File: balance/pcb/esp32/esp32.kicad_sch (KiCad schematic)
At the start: 3 parts

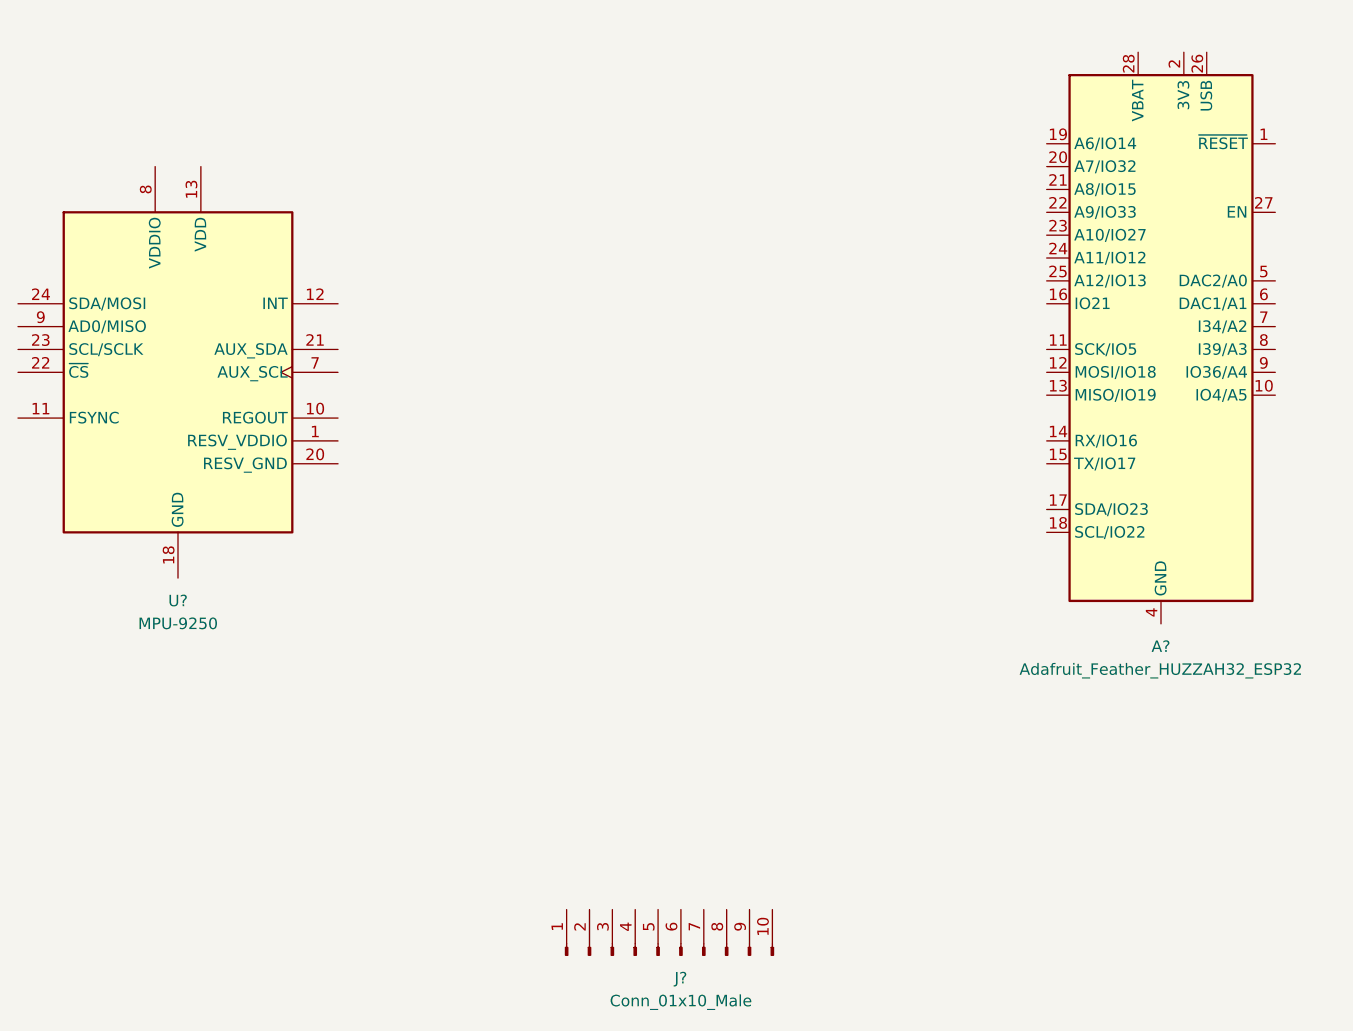
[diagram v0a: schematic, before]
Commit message: balance robot: power board
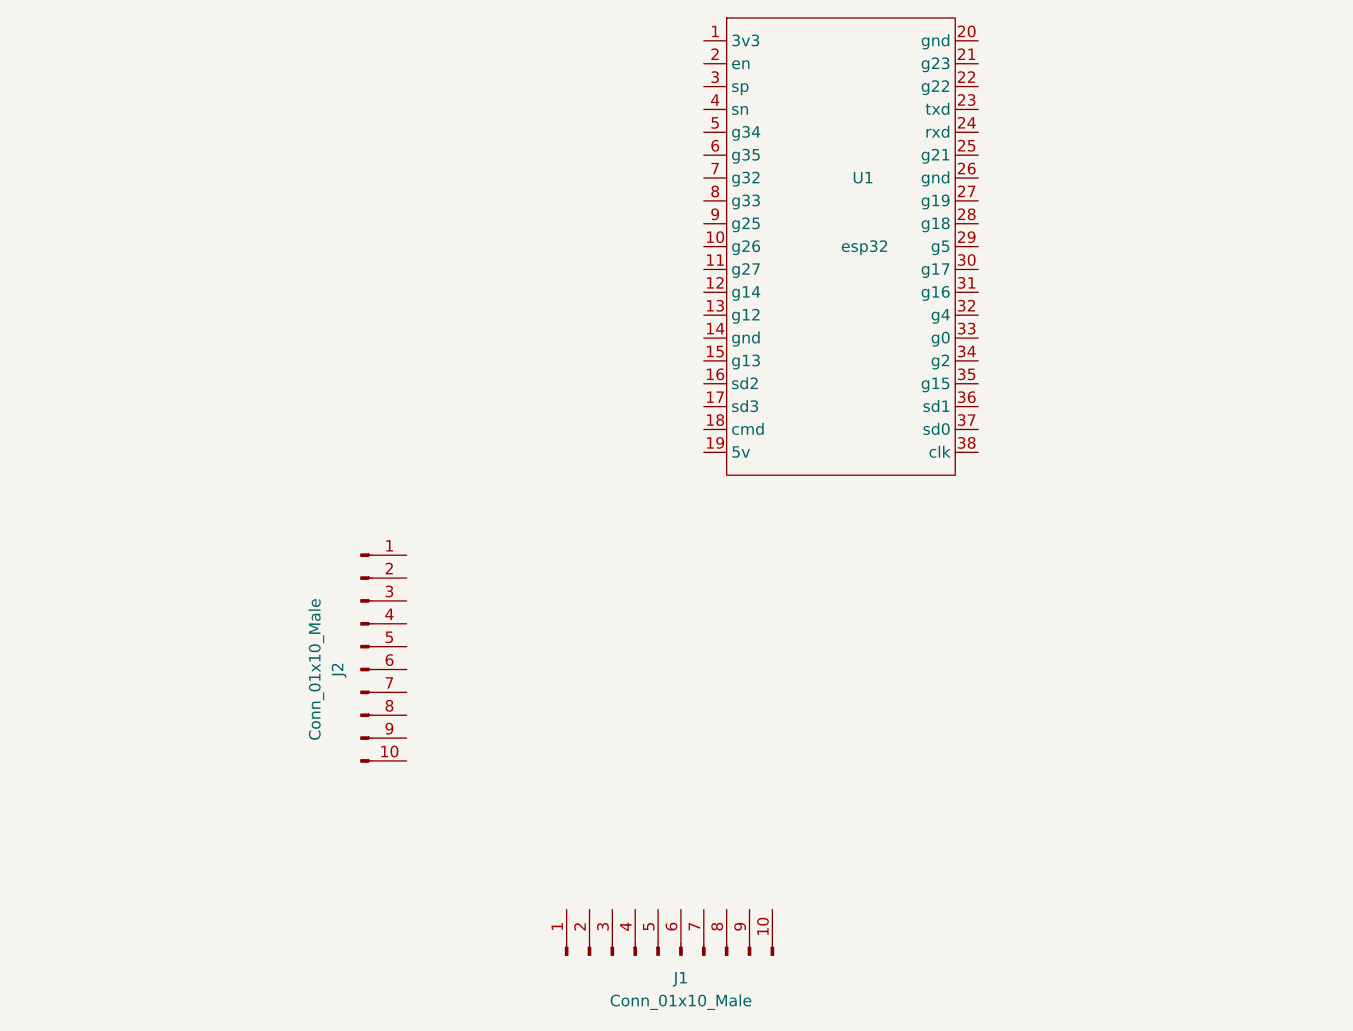
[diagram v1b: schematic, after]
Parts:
- removed A?: Adafruit_Feather_HUZZAH32_ESP32, Module:Adafruit_Feather, symbol MCU_Module:Adafruit_Feather_HUZZAH32_ESP32
- removed U?: MPU-9250, Sensor_Motion:InvenSense_QFN-24_3x3mm_P0.4mm, symbol Sensor_Motion:MPU-9250
- added J2: Conn_01x10_Male, Connector_PinHeader_2.54mm:PinHeader_1x10_P2.54mm_Vertical, symbol Connector:Conn_01x10_Male
- added U1: esp32, esp32:esp32, symbol esp32:esp32
- J1: renamed from J?; footprint (none) -> Connector_PinHeader_2.54mm:PinHeader_1x10_P2.54mm_Vertical
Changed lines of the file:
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@@
   (page 1 1)
   (paper "A4")
+  (symbol (lib_id "Connector:Conn_01x10_Male") (at 107.95 107.95 0) (unit 1)
+    (in_bom yes) (on_board yes)
+    (property "Reference" "J2" (id 0) (at 105.41 110.49 90))
+    (property "Value" "Conn_01x10_Male" (id 1) (at 102.87 110.49 90))
+    (property "Footprint" "Connector_PinHeader_2.54mm:PinHeader_1x10_P2.54mm_Vertical" (id 2) (at 107.95 107.95 0)
+      (effects (font (size 1.27 1.27)) hide)
+    )
+    (property "Datasheet" "~" (id 3) (at 107.95 107.95 0)
+      (effects (font (size 1.27 1.27)) hide)
+    )
+  )
   (symbol (lib_id "Connector:Conn_01x10_Male") (at 140.97 142.24 90) (unit 1)
     (in_bom yes) (on_board yes)
-    (property "Reference" "J?" (id 0) (at 143.51 144.78 90))
+    (property "Reference" "J1" (id 0) (at 143.51 144.78 90))
     (property "Value" "Conn_01x10_Male" (id 1) (at 143.51 147.32 90))
-    (property "Footprint" "" (id 2) (at 140.97 142.24 0)
+    (property "Footprint" "Connector_PinHeader_2.54mm:PinHeader_1x10_P2.54mm_Vertical" (id 2) (at 140.97 142.24 0)
       (effects (font (size 1.27 1.27)) hide)
     )
@@
     )
   )
-  (symbol (lib_id "MCU_Module:Adafruit_Feather_HUZZAH32_ESP32") (at 196.85 72.39 0) (unit 1)
+  (symbol (lib_id "esp32:esp32") (at 161.29 63.5 0) (unit 1)
     (in_bom yes) (on_board yes)
-    (property "Reference" "A?" (id 0) (at 196.85 107.95 0))
-    (property "Value" "Adafruit_Feather_HUZZAH32_ESP32" (id 1) (at 196.85 110.49 0))
-    (property "Footprint" "Module:Adafruit_Feather" (id 2) (at 199.39 106.68 0)
-      (effects (font (size 1.27 1.27)) (justify left) hide)
+    (property "Reference" "U1" (id 0) (at 162.56 55.88 0)
+      (effects (font (size 1.27 1.27)) (justify left))
     )
-    (property "Datasheet" "https://cdn-learn.adafruit.com/downloads/pdf/adafruit-huzzah32-esp32-feather.pdf" (id 3) (at 196.85 102.87 0)
+    (property "Value" "esp32" (id 1) (at 161.29 63.5 0)
+      (effects (font (size 1.27 1.27)) (justify left))
+    )
+    (property "Footprint" "esp32:esp32" (id 2) (at 161.29 63.5 0)
       (effects (font (size 1.27 1.27)) hide)
     )
-  )
-  (symbol (lib_id "Sensor_Motion:MPU-9250") (at 87.63 77.47 0) (unit 1)
-    (in_bom yes) (on_board yes)
-    (property "Reference" "U?" (id 0) (at 87.63 102.87 0))
-    (property "Value" "MPU-9250" (id 1) (at 87.63 105.41 0))
-    (property "Footprint" "Sensor_Motion:InvenSense_QFN-24_3x3mm_P0.4mm" (id 2) (at 87.63 102.87 0)
-      (effects (font (size 1.27 1.27)) hide)
-    )
-    (property "Datasheet" "https://store.invensense.com/datasheets/invensense/MPU9250REV1.0.pdf" (id 3) (at 87.63 81.28 0)
+    (property "Datasheet" "" (id 3) (at 161.29 63.5 0)
       (effects (font (size 1.27 1.27)) hide)
     )
@@
   )
   (symbol_instances
-    (path "/a5b746d2-1695-4135-8a8f-f725738ad230"
-      (reference "A?") (unit 1) (value "Adafruit_Feather_HUZZAH32_ESP32") (footprint "Module:Adafruit_Feather")
+    (path "/ea9d1a73-9cbe-4214-b621-565aab468fb0"
+      (reference "J1") (unit 1) (value "Conn_01x10_Male") (footprint "Connector_PinHeader_2.54mm:PinHeader_1x10_P2.54mm_Vertical")
     )
-    (path "/ea9d1a73-9cbe-4214-b621-565aab468fb0"
-      (reference "J?") (unit 1) (value "Conn_01x10_Male") (footprint "")
+    (path "/4264ba5f-12a7-4bed-b9ea-1dfc4ad2a5da"
+      (reference "J2") (unit 1) (value "Conn_01x10_Male") (footprint "Connector_PinHeader_2.54mm:PinHeader_1x10_P2.54mm_Vertical")
     )
-    (path "/d1e24ed7-8926-4aaf-b61d-e40939a55b8d"
-      (reference "U?") (unit 1) (value "MPU-9250") (footprint "Sensor_Motion:InvenSense_QFN-24_3x3mm_P0.4mm")
+    (path "/7e8e1615-5e4b-4d77-a706-9692524d14b7"
+      (reference "U1") (unit 1) (value "esp32") (footprint "esp32:esp32")
     )
   )
